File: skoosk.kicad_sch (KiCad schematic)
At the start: 92 parts, among them SW1 SW_Push, SW2 RotaryEncoder_Switch, U1 ProMicro

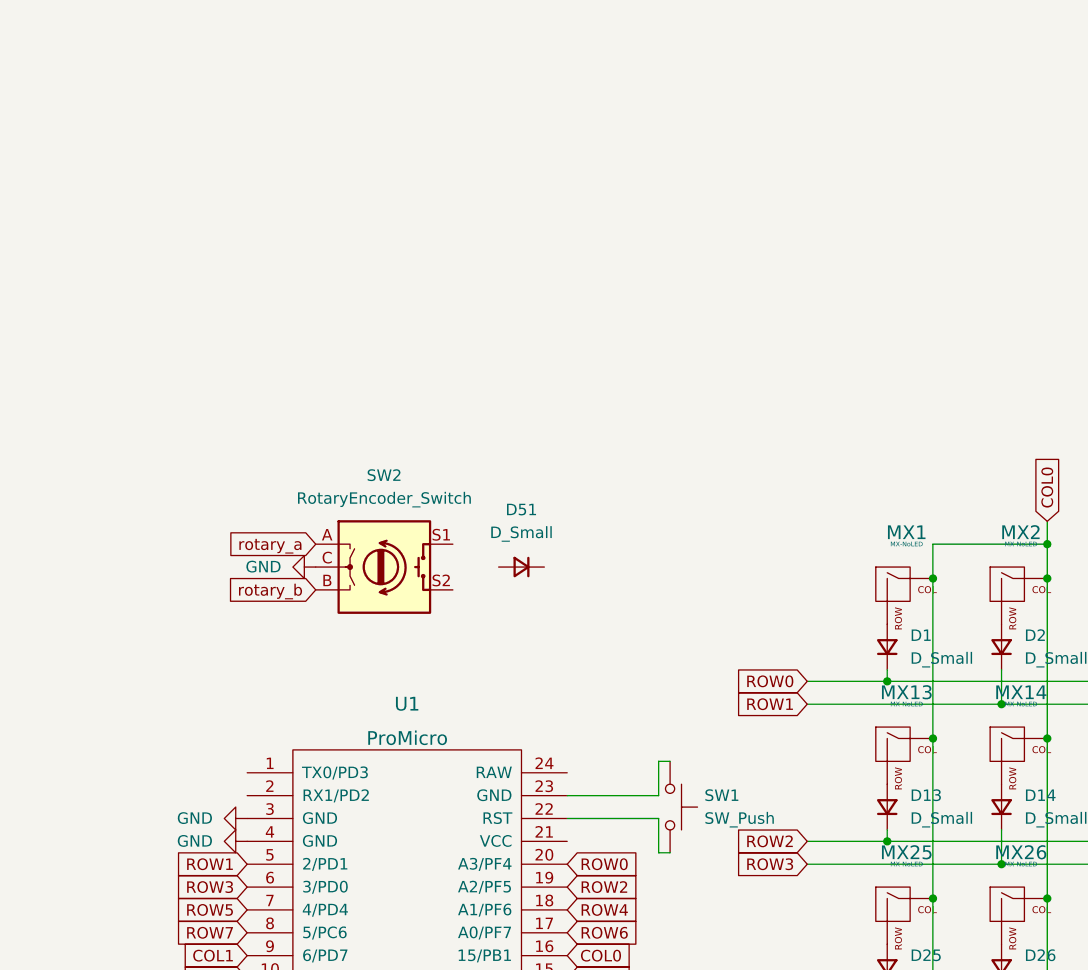
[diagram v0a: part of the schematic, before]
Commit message: added rotary and rgb to schematics and editor
not yet fully confirmed to be working correctly
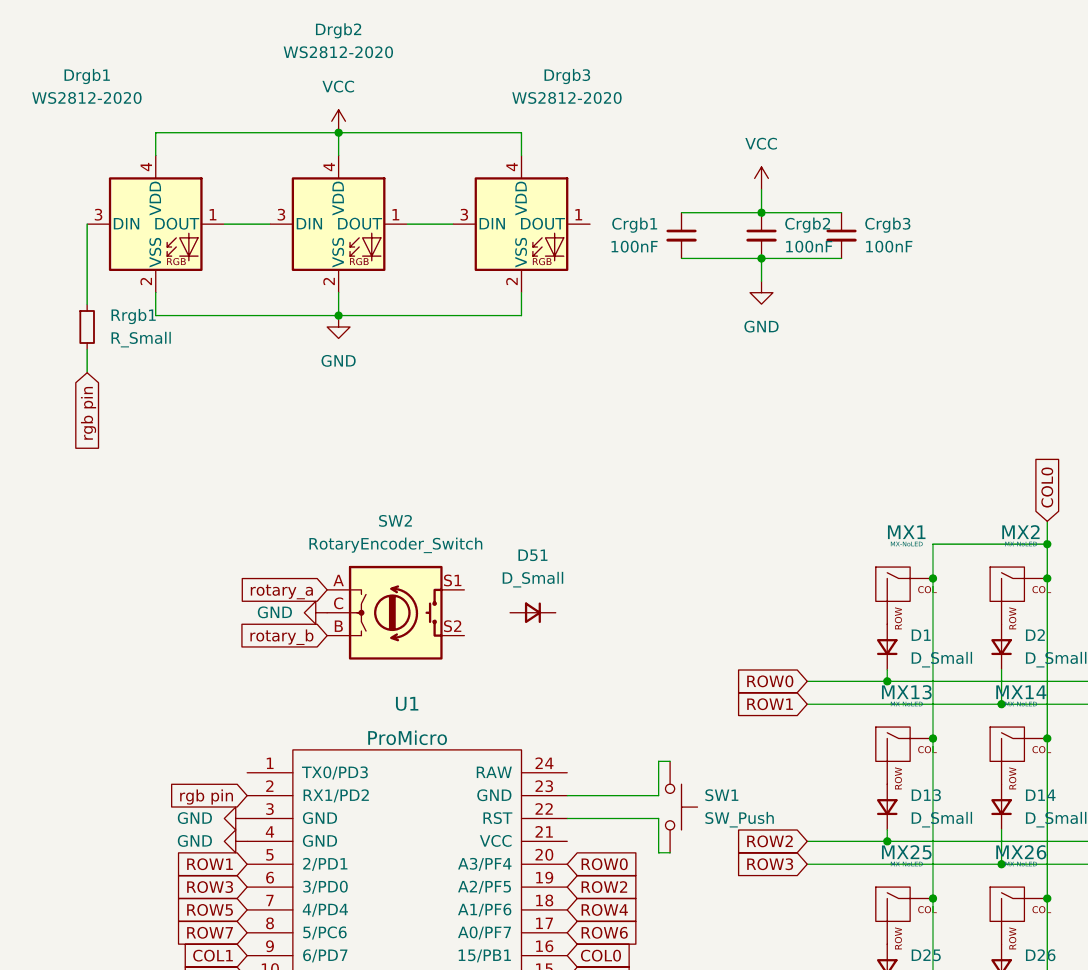
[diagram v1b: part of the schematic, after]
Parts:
- added Crgb1, Crgb2, Crgb3: 100nF, Capacitor_THT:C_Disc_D3.0mm_W1.6mm_P2.50mm, symbol Device:C_Small
- added Drgb1, Drgb2, Drgb3: WS2812-2020, CrumpPrints:WS2812-2020, symbol crumpschemes:WS2812-2020
- added Rrgb1: R_Small, Resistor_THT:R_Axial_DIN0204_L3.6mm_D1.6mm_P5.08mm_Horizontal, symbol Device:R_Small
- D51: footprint (none) -> Diode_THT:D_DO-35_SOD27_P7.62mm_Horizontal
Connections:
- net GND: now also Crgb1.2, Crgb2.2, Crgb3.2, Drgb1.2 (VSS), Drgb2.2 (VSS), Drgb3.2 (VSS)
- net rgb pin: now reaches U1.2 (RX1/PD2)
- net rgb pin: now also Rrgb1.2
- new net: Drgb2.1 (DOUT), Drgb3.3 (DIN)
- new net: Drgb1.1 (DOUT), Drgb2.3 (DIN)
- new net: Drgb1.3 (DIN), Rrgb1.1
- new net VCC: Crgb1.1, Crgb2.1, Crgb3.1, Drgb1.4 (VDD), Drgb2.4 (VDD), Drgb3.4 (VDD)
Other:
- moved on the sheet: D51, SW2

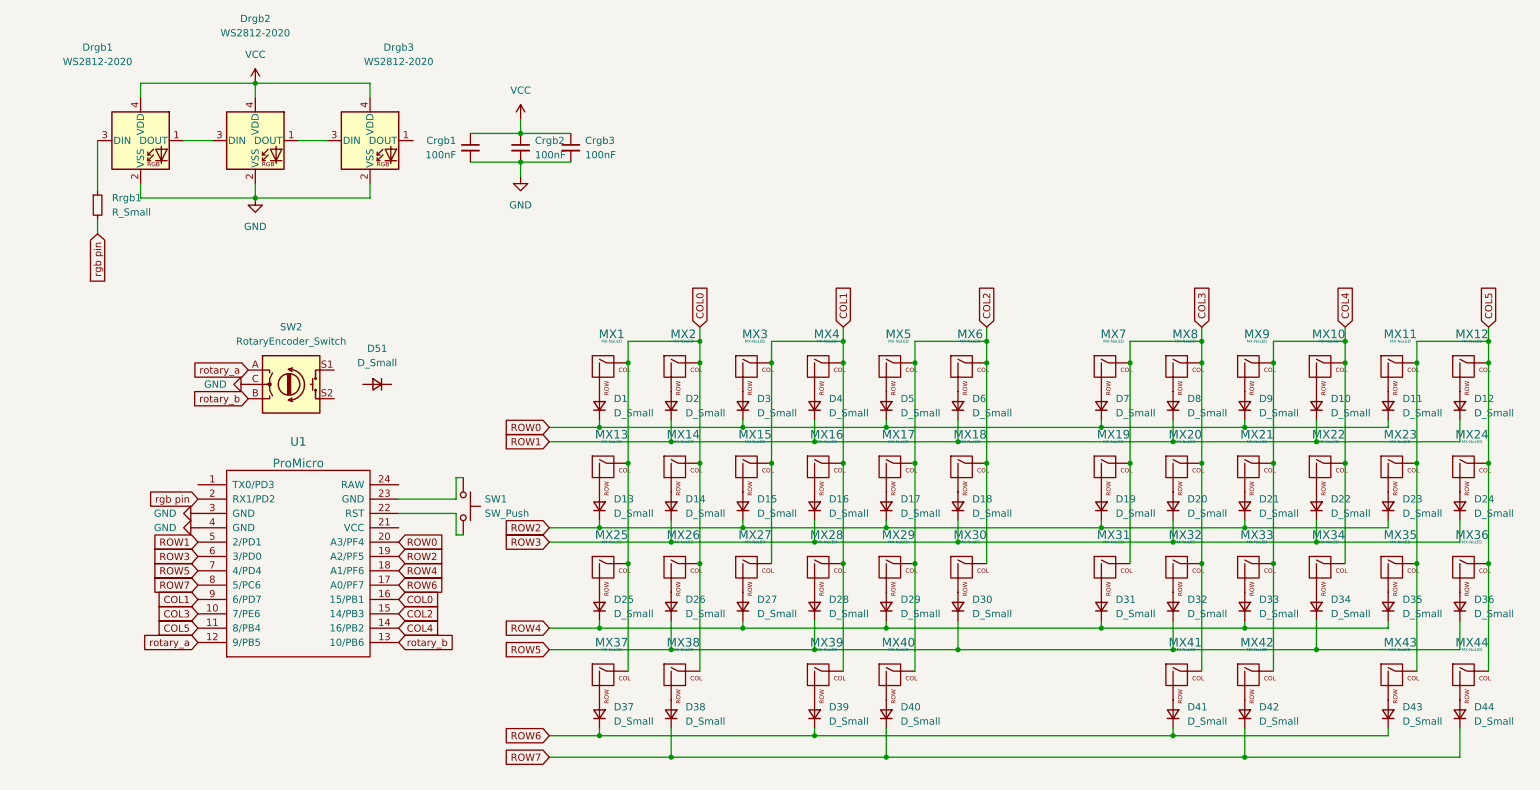
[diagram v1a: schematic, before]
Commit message: rotary schematics updated, smd capacitors chosen for rgb
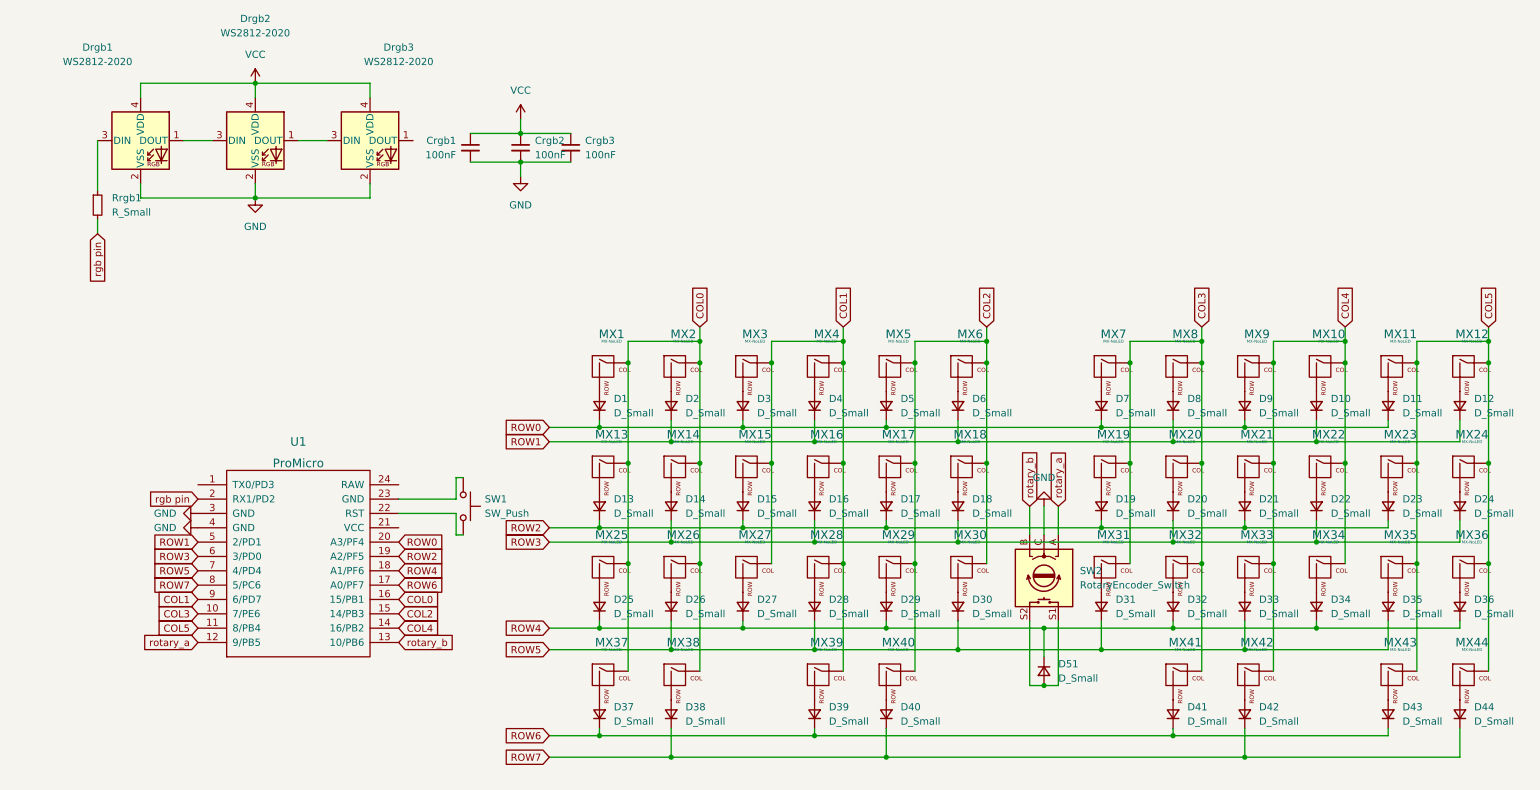
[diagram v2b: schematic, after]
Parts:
- Crgb1, Crgb2, Crgb3: footprint Capacitor_THT:C_Disc_D3.0mm_W1.6mm_P2.50mm -> Capacitor_SMD:C_0402_1005Metric
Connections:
- net ROW4: now also D32.1 (K), D34.1 (K), D36.1 (K), D51.1 (K); no longer D31.1 (K), D33.1 (K), D35.1 (K)
- net ROW5: now also D31.1 (K), D33.1 (K), D35.1 (K); no longer D32.1 (K), D34.1 (K), D36.1 (K)
- net at SW2.S1: now also D51.2 (A), SW2.S2
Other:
- moved on the sheet: D51, SW2

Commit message: fixed schematics
new routing to be done
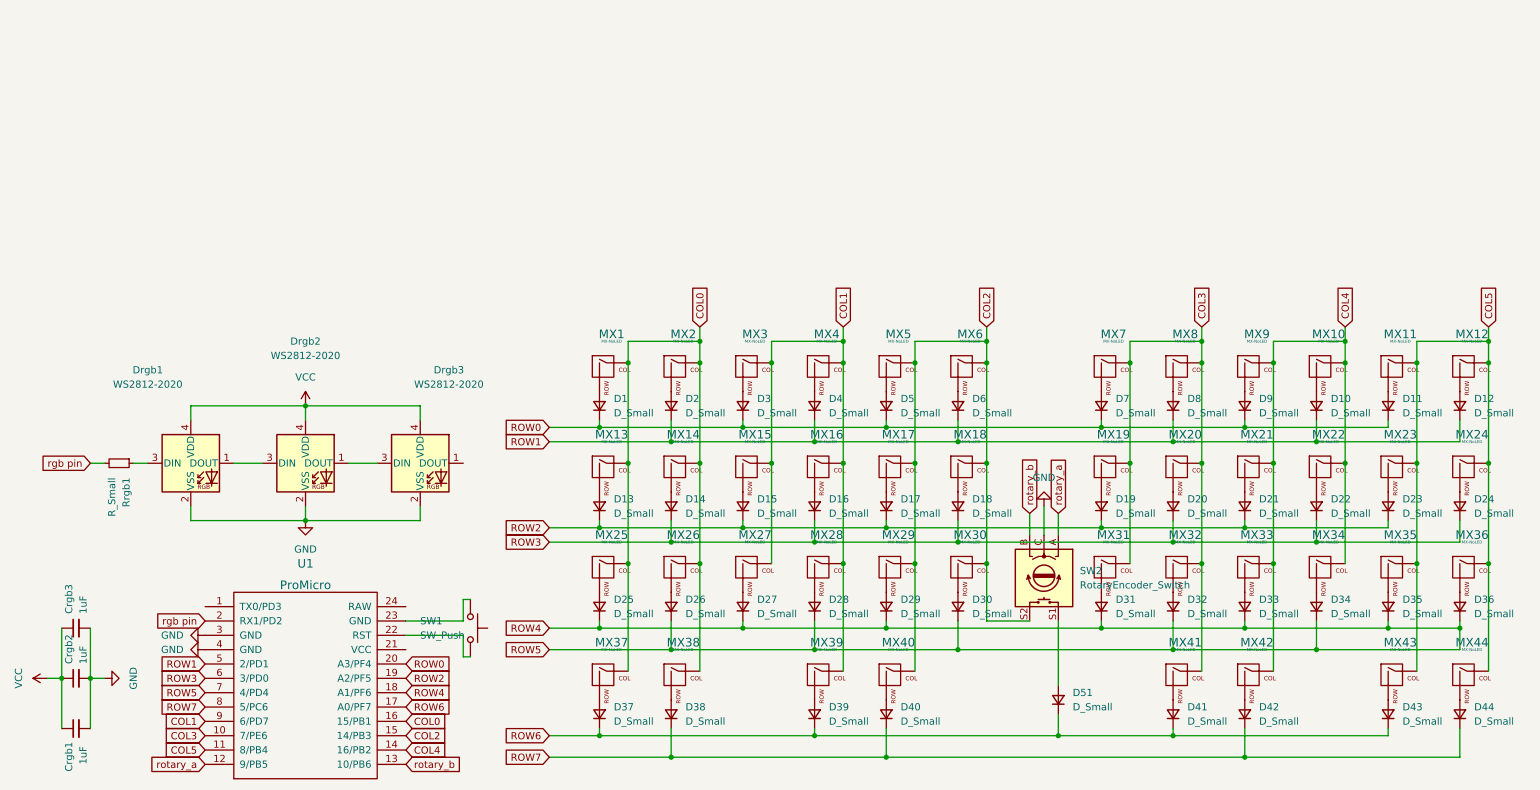
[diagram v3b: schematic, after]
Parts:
- Crgb1, Crgb2, Crgb3: value 100nF -> 1uF
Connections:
- net ROW5 is gone; now on net ROW4: D26.1 (K), D28.1 (K), D30.1 (K), D31.1 (K), D33.1 (K), D35.1 (K), U1.7 (4/PD4)
- net COL2: now also SW2.S2
- net ROW4: no longer D51.1 (K)
- net ROW6: now also D51.1 (K)
- net at D51.2 (A), SW2.S1: no longer SW2.S2
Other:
- moved on the sheet: Crgb1, Crgb2, Crgb3, D51, Drgb1, Drgb2, Drgb3, Rrgb1, SW1, U1

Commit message: final fix to schematic
noah approved
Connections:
- net GND: now also SW1.1, U1.23 (GND)
- net VCC: now also U1.21 (VCC)
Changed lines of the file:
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@@
   (junction (at 120.65 109.22) (diameter 0) (color 0 0 0 0)
   )
+  (junction (at 92.71 115.57) (diameter 0) (color 0 0 0 0)
+  )
   (junction (at 20.32 129.54) (diameter 0) (color 0 0 0 0)
   )
@@
   )
   (wire (pts (xy 217.17 87.63) (xy 242.57 87.63))
+    (stroke (width 0) (type default) (color 0 0 0 0))
+  )
+  (wire (pts (xy 92.71 115.57) (xy 96.52 115.57))
     (stroke (width 0) (type default) (color 0 0 0 0))
   )
@@
     (pin "1")
     (pin "2")
+  )
+  (symbol (lib_id "power:GND") (at 96.52 115.57 90) (unit 1)
+    (in_bom yes) (on_board yes) (fields_autoplaced)
+    (property "Reference" "#PWR?" (id 0) (at 102.87 115.57 0)
+      (effects (font (size 1.27 1.27)) hide)
+    )
+    (property "Value" "GND" (id 1) (at 100.33 115.5699 90)
+      (effects (font (size 1.27 1.27)) (justify right))
+    )
+    (property "Footprint" "" (id 2) (at 96.52 115.57 0)
+      (effects (font (size 1.27 1.27)) hide)
+    )
+    (property "Datasheet" "" (id 3) (at 96.52 115.57 0)
+      (effects (font (size 1.27 1.27)) hide)
+    )
+    (pin "1")
   )
   (symbol (lib_id "Device:D_Small") (at 128.27 99.06 90) (unit 1)
@@
     (pin "9")
   )
+  (symbol (lib_id "power:VCC") (at 81.28 124.46 270) (unit 1)
+    (in_bom yes) (on_board yes) (fields_autoplaced)
+    (property "Reference" "#PWR?" (id 0) (at 77.47 124.46 0)
+      (effects (font (size 1.27 1.27)) hide)
+    )
+    (property "Value" "VCC" (id 1) (at 85.09 124.4599 90)
+      (effects (font (size 1.27 1.27)) (justify left))
+    )
+    (property "Footprint" "" (id 2) (at 81.28 124.46 0)
+      (effects (font (size 1.27 1.27)) hide)
+    )
+    (property "Datasheet" "" (id 3) (at 81.28 124.46 0)
+      (effects (font (size 1.27 1.27)) hide)
+    )
+    (pin "1")
+  )
   (symbol (lib_id "MX_Alps_Hybrid:MX-NoLED") (at 167.64 74.93 0) (unit 1)
     (in_bom yes) (on_board yes) (fields_autoplaced)
@@
       (reference "#PWR0107") (unit 1) (value "GND") (footprint "")
     )
+    (path "/835fe862-bf49-4aad-bdd0-ce0a95cfa8b5"
+      (reference "#PWR?") (unit 1) (value "GND") (footprint "")
+    )
+    (path "/b57599e0-cc1b-4059-9798-8cf61dd07e0a"
+      (reference "#PWR?") (unit 1) (value "VCC") (footprint "")
+    )
     (path "/2b760963-b83c-46c2-8661-fa7bfb8e7615"

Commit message: changed layout for pcb, switch and backplate. added curved routes
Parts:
- MX1, MX12, MX13, MX24, MX25, MX36, MX37, MX44: footprint MX_Only:MXOnly-1.25U-NoLED -> MX_Only:MXOnly-1U-NoLED
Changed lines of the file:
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@@
       (effects (font (size 0.508 0.508)))
     )
-    (property "Footprint" "MX_Only:MXOnly-1.25U-NoLED" (id 2) (at 100.965 111.125 0)
+    (property "Footprint" "MX_Only:MXOnly-1U-NoLED" (id 2) (at 100.965 111.125 0)
       (effects (font (size 1.524 1.524)) hide)
     )
@@
       (effects (font (size 0.508 0.508)))
     )
-    (property "Footprint" "MX_Only:MXOnly-1.25U-NoLED" (id 2) (at 100.965 75.565 0)
+    (property "Footprint" "MX_Only:MXOnly-1U-NoLED" (id 2) (at 100.965 75.565 0)
       (effects (font (size 1.524 1.524)) hide)
     )
@@
       (effects (font (size 0.508 0.508)))
     )
-    (property "Footprint" "MX_Only:MXOnly-1.25U-NoLED" (id 2) (at 100.965 93.345 0)
+    (property "Footprint" "MX_Only:MXOnly-1U-NoLED" (id 2) (at 100.965 93.345 0)
       (effects (font (size 1.524 1.524)) hide)
     )
@@
   (symbol (lib_id "power:GND") (at 96.52 115.57 90) (unit 1)
     (in_bom yes) (on_board yes) (fields_autoplaced)
-    (property "Reference" "#PWR?" (id 0) (at 102.87 115.57 0)
+    (property "Reference" "#PWR0109" (id 0) (at 102.87 115.57 0)
       (effects (font (size 1.27 1.27)) hide)
     )
@@
   (symbol (lib_id "power:VCC") (at 81.28 124.46 270) (unit 1)
     (in_bom yes) (on_board yes) (fields_autoplaced)
-    (property "Reference" "#PWR?" (id 0) (at 77.47 124.46 0)
+    (property "Reference" "#PWR0108" (id 0) (at 77.47 124.46 0)
       (effects (font (size 1.27 1.27)) hide)
     )
@@
       (effects (font (size 0.508 0.508)))
     )
-    (property "Footprint" "MX_Only:MXOnly-1.25U-NoLED" (id 2) (at 253.365 130.175 0)
+    (property "Footprint" "MX_Only:MXOnly-1U-NoLED" (id 2) (at 253.365 130.175 0)
       (effects (font (size 1.524 1.524)) hide)
     )
@@
       (effects (font (size 0.508 0.508)))
     )
-    (property "Footprint" "MX_Only:MXOnly-1.25U-NoLED" (id 2) (at 253.365 111.125 0)
+    (property "Footprint" "MX_Only:MXOnly-1U-NoLED" (id 2) (at 253.365 111.125 0)
       (effects (font (size 1.524 1.524)) hide)
     )
@@
       (effects (font (size 0.508 0.508)))
     )
-    (property "Footprint" "MX_Only:MXOnly-1.25U-NoLED" (id 2) (at 253.365 75.565 0)
+    (property "Footprint" "MX_Only:MXOnly-1U-NoLED" (id 2) (at 253.365 75.565 0)
       (effects (font (size 1.524 1.524)) hide)
     )
@@
       (effects (font (size 0.508 0.508)))
     )
-    (property "Footprint" "MX_Only:MXOnly-1.25U-NoLED" (id 2) (at 100.965 130.175 0)
+    (property "Footprint" "MX_Only:MXOnly-1U-NoLED" (id 2) (at 100.965 130.175 0)
       (effects (font (size 1.524 1.524)) hide)
     )
@@
       (effects (font (size 0.508 0.508)))
     )
-    (property "Footprint" "MX_Only:MXOnly-1.25U-NoLED" (id 2) (at 253.365 93.345 0)
+    (property "Footprint" "MX_Only:MXOnly-1U-NoLED" (id 2) (at 253.365 93.345 0)
       (effects (font (size 1.524 1.524)) hide)
     )
@@
       (reference "#PWR0107") (unit 1) (value "GND") (footprint "")
     )
+    (path "/b57599e0-cc1b-4059-9798-8cf61dd07e0a"
+      (reference "#PWR0108") (unit 1) (value "VCC") (footprint "")
+    )
     (path "/835fe862-bf49-4aad-bdd0-ce0a95cfa8b5"
-      (reference "#PWR?") (unit 1) (value "GND") (footprint "")
-    )
-    (path "/b57599e0-cc1b-4059-9798-8cf61dd07e0a"
-      (reference "#PWR?") (unit 1) (value "VCC") (footprint "")
+      (reference "#PWR0109") (unit 1) (value "GND") (footprint "")
     )
     (path "/2b760963-b83c-46c2-8661-fa7bfb8e7615"
@@
     )
     (path "/06d6f48f-e469-4354-9f3f-73c3c7e47130"
-      (reference "MX1") (unit 1) (value "MX-NoLED") (footprint "MX_Only:MXOnly-1.25U-NoLED")
+      (reference "MX1") (unit 1) (value "MX-NoLED") (footprint "MX_Only:MXOnly-1U-NoLED")
     )
     (path "/2fb00450-c725-4180-b979-d28a252e6ae8"
@@
     )
     (path "/db06471a-f536-4b29-8218-cf849310797a"
-      (reference "MX12") (unit 1) (value "MX-NoLED") (footprint "MX_Only:MXOnly-1.25U-NoLED")
+      (reference "MX12") (unit 1) (value "MX-NoLED") (footprint "MX_Only:MXOnly-1U-NoLED")
     )
     (path "/7b455f67-bf00-4bff-a7c2-40cd7dbc6d98"
-      (reference "MX13") (unit 1) (value "MX-NoLED") (footprint "MX_Only:MXOnly-1.25U-NoLED")
+      (reference "MX13") (unit 1) (value "MX-NoLED") (footprint "MX_Only:MXOnly-1U-NoLED")
     )
     (path "/76371a8c-20ef-42e4-97de-502d07a69f89"
@@
     )
     (path "/e1941a19-abb6-4102-a2a6-af1685d6b19e"
-      (reference "MX24") (unit 1) (value "MX-NoLED") (footprint "MX_Only:MXOnly-1.25U-NoLED")
+      (reference "MX24") (unit 1) (value "MX-NoLED") (footprint "MX_Only:MXOnly-1U-NoLED")
     )
     (path "/01b25cf9-37a6-406e-a967-fb60f3ceb24d"
-      (reference "MX25") (unit 1) (value "MX-NoLED") (footprint "MX_Only:MXOnly-1.25U-NoLED")
+      (reference "MX25") (unit 1) (value "MX-NoLED") (footprint "MX_Only:MXOnly-1U-NoLED")
     )
     (path "/2a3b66a8-d0e7-4bf3-86cd-8903c6212fc1"
@@
     )
     (path "/d3161ab3-a226-4a34-b0de-246ca221f66e"
-      (reference "MX36") (unit 1) (value "MX-NoLED") (footprint "MX_Only:MXOnly-1.25U-NoLED")
+      (reference "MX36") (unit 1) (value "MX-NoLED") (footprint "MX_Only:MXOnly-1U-NoLED")
     )
     (path "/e0ac9420-96d7-4f5e-b000-b0d14e7aaced"
-      (reference "MX37") (unit 1) (value "MX-NoLED") (footprint "MX_Only:MXOnly-1.25U-NoLED")
+      (reference "MX37") (unit 1) (value "MX-NoLED") (footprint "MX_Only:MXOnly-1U-NoLED")
     )
     (path "/6056c5db-1ad2-46d7-92ac-51e7fb050623"
@@
     )
     (path "/cd39db94-3d7c-46bf-8554-509aa6ee1aa3"
-      (reference "MX44") (unit 1) (value "MX-NoLED") (footprint "MX_Only:MXOnly-1.25U-NoLED")
+      (reference "MX44") (unit 1) (value "MX-NoLED") (footprint "MX_Only:MXOnly-1U-NoLED")
     )
     (path "/fbc2eaac-d9a0-45ae-9516-ef1321b60b11"
